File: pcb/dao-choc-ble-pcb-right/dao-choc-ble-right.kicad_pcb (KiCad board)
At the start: 2 copper layers, 150 x 85.7 mm, 85 parts, among them J1 USB, J2 PROG, K1 KEY_SWITCH, K10 KEY_SWITCH, K11 KEY_SWITCH, K12 KEY_SWITCH, K13 KEY_SWITCH, K14 KEY_SWITCH, K15 KEY_SWITCH, K16 KEY_SWITCH, K17 KEY_SWITCH, K18 KEY_SWITCH, K19 KEY_SWITCH, K2 KEY_SWITCH, K20 KEY_SWITCH, K21 KEY_SWITCH, K22 KEY_SWITCH, K3 KEY_SWITCH, K4 KEY_SWITCH, K5 KEY_SWITCH, K6 KEY_SWITCH, K7 KEY_SWITCH, K8 KEY_SWITCH, K9 KEY_SWITCH, Q1 AO3401A, SW1 ON_OFF, SW2 RESET, U1 MS88SF2, U2 USBLC6-2SC6, U3 XC6220, U4 MCP73831

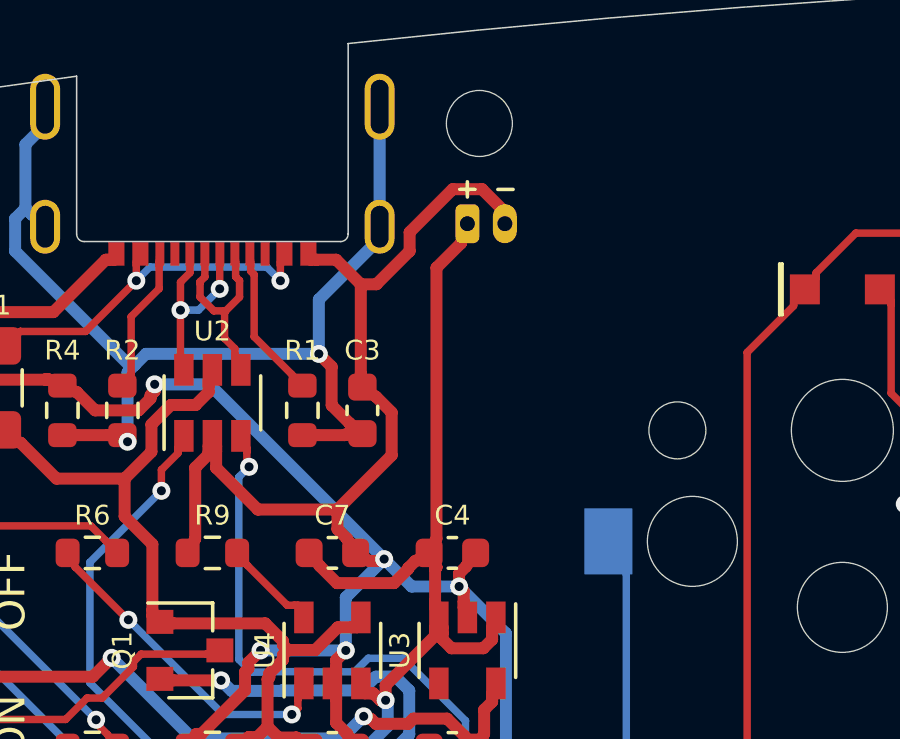
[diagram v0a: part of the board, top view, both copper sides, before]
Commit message: feature: changed footprint for battery connector
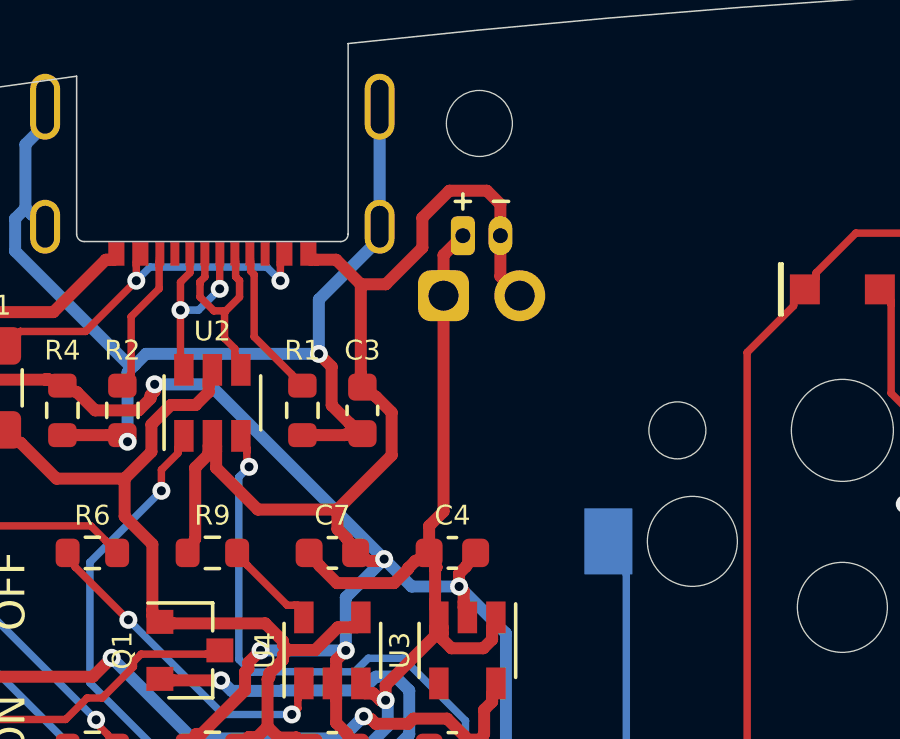
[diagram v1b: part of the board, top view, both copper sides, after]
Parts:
- moved BT1 0.43 mm to (152.3, -4.71)
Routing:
- net GND: track 152.9 -> 155.8 mm
